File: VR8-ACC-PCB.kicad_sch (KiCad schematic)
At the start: 41 parts, among them IC1 LM393P, IC2 VO14642AT, IC3 VO14642AT, IC4 KT12-1A-40L-THT, IC5 NE555P, Q1 Q_NMOS_Depletion_GDS, Q2 Q_NMOS_Depletion_GDS, Q3 Q_NMOS_Depletion_GDS

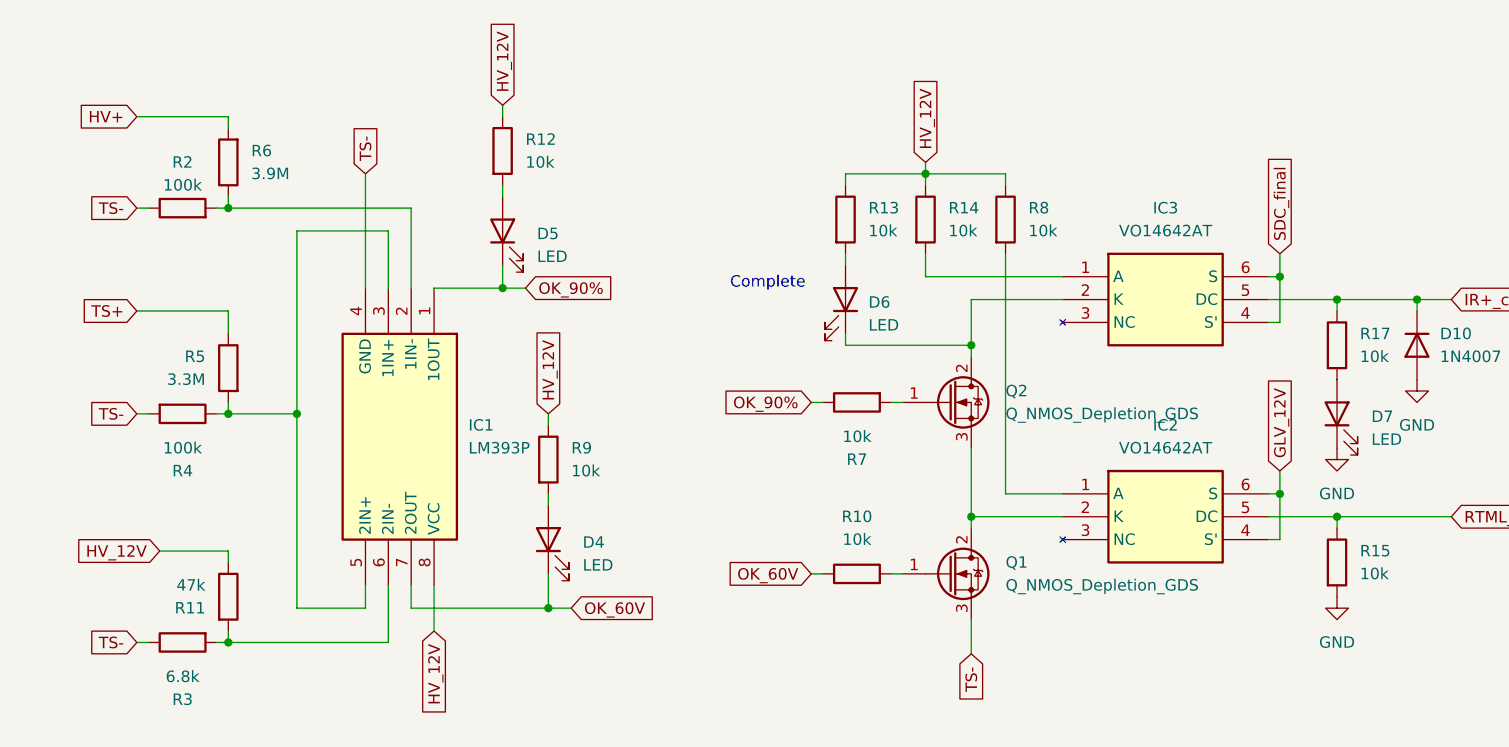
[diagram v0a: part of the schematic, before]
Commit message: add mouser part numbers
change resisters footprints of 0805 to 1206 for 500V voltage rating
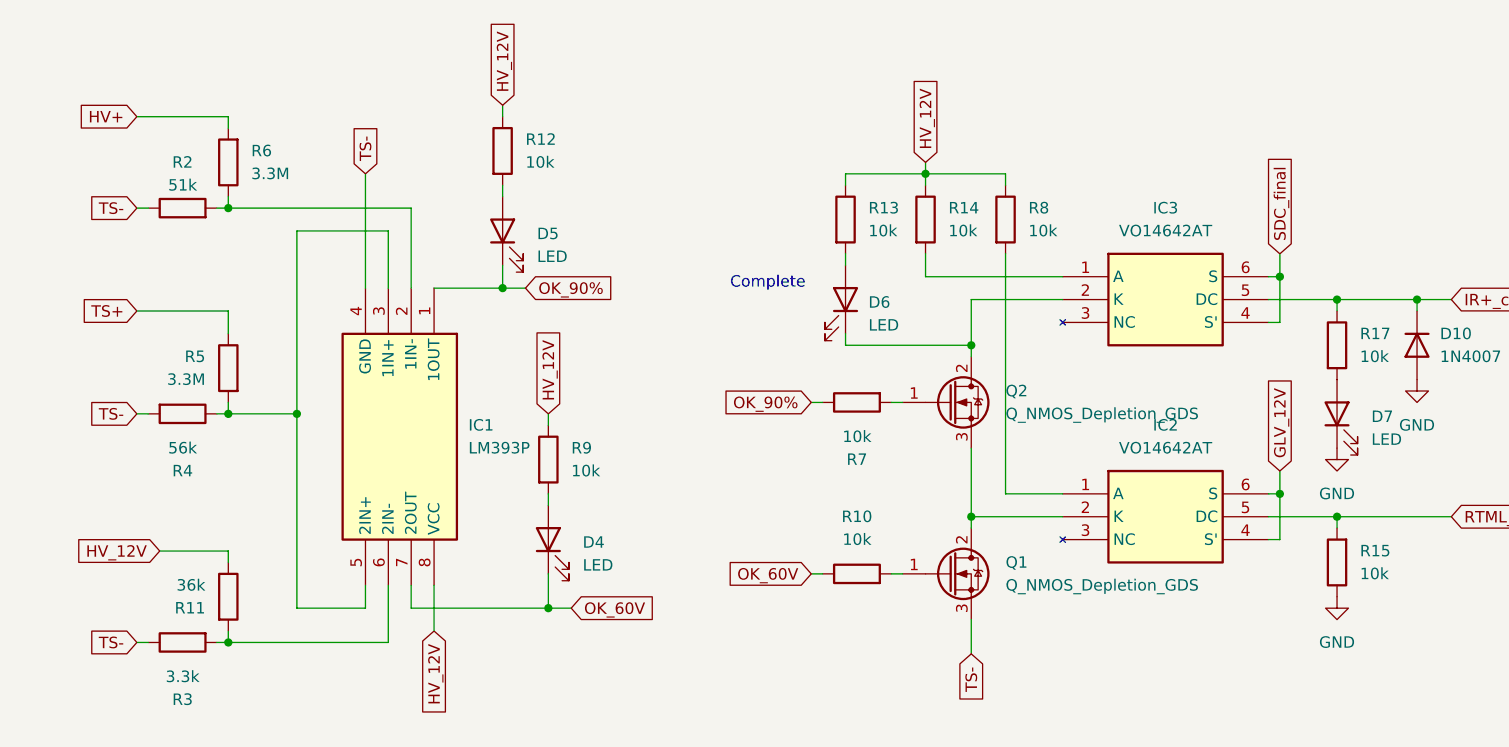
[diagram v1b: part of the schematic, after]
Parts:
- C1: Manufacturer_Part_Number (none) -> 0805B103K101CT; Mouser Part Number (none) -> 791-0805B103K101CT
- C2: Manufacturer_Part_Number (none) -> 0805X475K160CT; Mouser Part Number (none) -> 791-0805X475K160CT
- D10, D11: Mouser Part Number (none) -> 637-1N4007
- D3: Manufacturer_Part_Number (none) -> 1N4759A-TAP; Mouser Part Number (none) -> 78-1N4759A-TAP
- F4: Manufacturer_Part_Number (none) -> 0ADKP1000-RE; Mouser Part Number (none) -> 530-0ADKP1000-RE
- Q1, Q2, Q3: Manufacturer_Part_Number (none) -> IPS70R1K4P7SAKMA1; Mouser Part Number (none) -> 726-IPS70R1K4P7AKMA1
- R10, R12, R13, R14, R15, R16, R17, R19, R7, R8, R9: footprint Resistor_SMD:R_0805_2012Metric_Pad1.20x1.40mm_HandSolder -> Resistor_SMD:R_1206_3216Metric_Pad1.30x1.75mm_HandSolder; Mouser Part Number (none) -> 667-ERJ-P08J103V
- R11: value 47k -> 36k; footprint Resistor_SMD:R_0805_2012Metric_Pad1.20x1.40mm_HandSolder -> Resistor_SMD:R_1206_3216Metric_Pad1.30x1.75mm_HandSolder; Mouser Part Number (none) -> 667-ERJ-P08J363V
- R18: footprint Resistor_SMD:R_0805_2012Metric_Pad1.20x1.40mm_HandSolder -> Resistor_SMD:R_1206_3216Metric_Pad1.30x1.75mm_HandSolder; Mouser Part Number (none) -> 667-ERJ-P08J473V
- R2: value 100k -> 51k; footprint Resistor_SMD:R_0805_2012Metric_Pad1.20x1.40mm_HandSolder -> Resistor_SMD:R_1206_3216Metric_Pad1.30x1.75mm_HandSolder; Mouser Part Number (none) -> 667-ERJ-P08J513V
- R21: footprint Resistor_SMD:R_0805_2012Metric_Pad1.20x1.40mm_HandSolder -> Resistor_SMD:R_1206_3216Metric_Pad1.30x1.75mm_HandSolder; Mouser Part Number (none) -> 667-ERJ-P08J102V
- R3: value 6.8k -> 3.3k; footprint Resistor_SMD:R_0805_2012Metric_Pad1.20x1.40mm_HandSolder -> Resistor_SMD:R_1206_3216Metric_Pad1.30x1.75mm_HandSolder; Mouser Part Number (none) -> 667-ERJ-P08J332V
- R4: value 100k -> 56k; footprint Resistor_SMD:R_0805_2012Metric_Pad1.20x1.40mm_HandSolder -> Resistor_SMD:R_1206_3216Metric_Pad1.30x1.75mm_HandSolder; Mouser Part Number (none) -> 667-ERJ-P08J563V
- R5: Mouser Part Number (none) -> 667-ERJ-P08J335V
- R6: value 3.9M -> 3.3M; Mouser Part Number (none) -> 667-ERJ-P08J335V
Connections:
- net GND: now also R15.1; no longer R15.2
- net RTML_enable: now also R15.2; no longer R15.1
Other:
- title: Acc PCB -> VR8-Acc-PCB
- moved on the sheet: R15
